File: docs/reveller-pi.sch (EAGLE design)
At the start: 21 parts, among them IC100 6581, Q100 IRF9Z24N, T100 BC547, X100 RASPI_BOARD_AB_E0, X101 PG203J, X102 CANTON-POWER

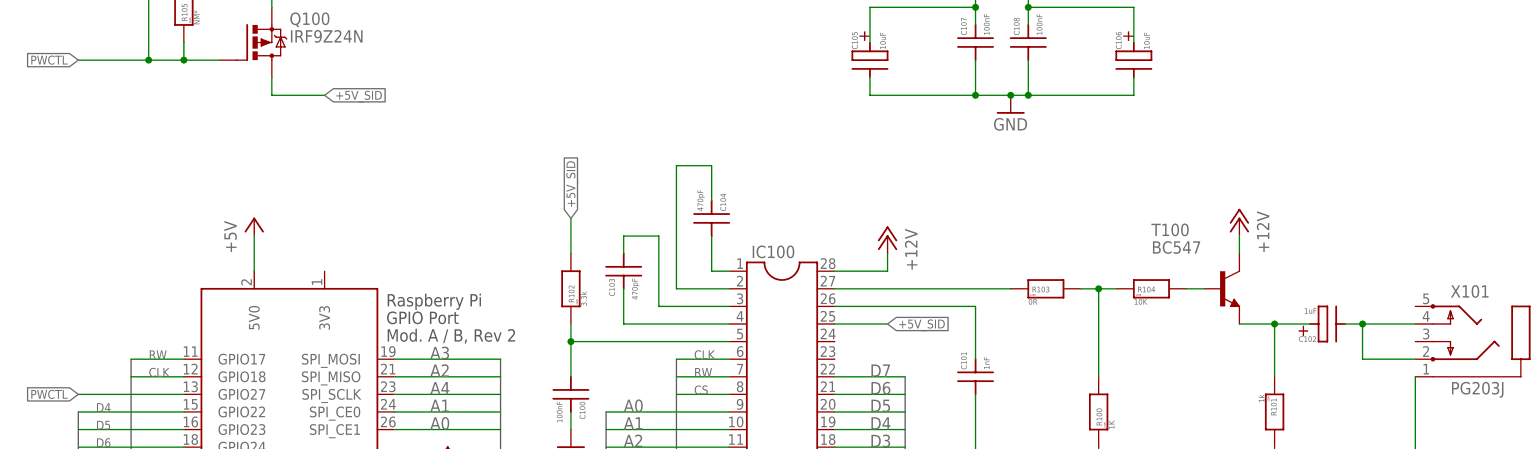
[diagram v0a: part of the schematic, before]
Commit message: Changed schmatic to allow for "stereo" sound
Used wrong pinout on jack connector, thereby giving only mono sound.
Also added one 1000uF capacitor to allow for bad powersupplys to not
kill the raspberrypi during startup of sidchip
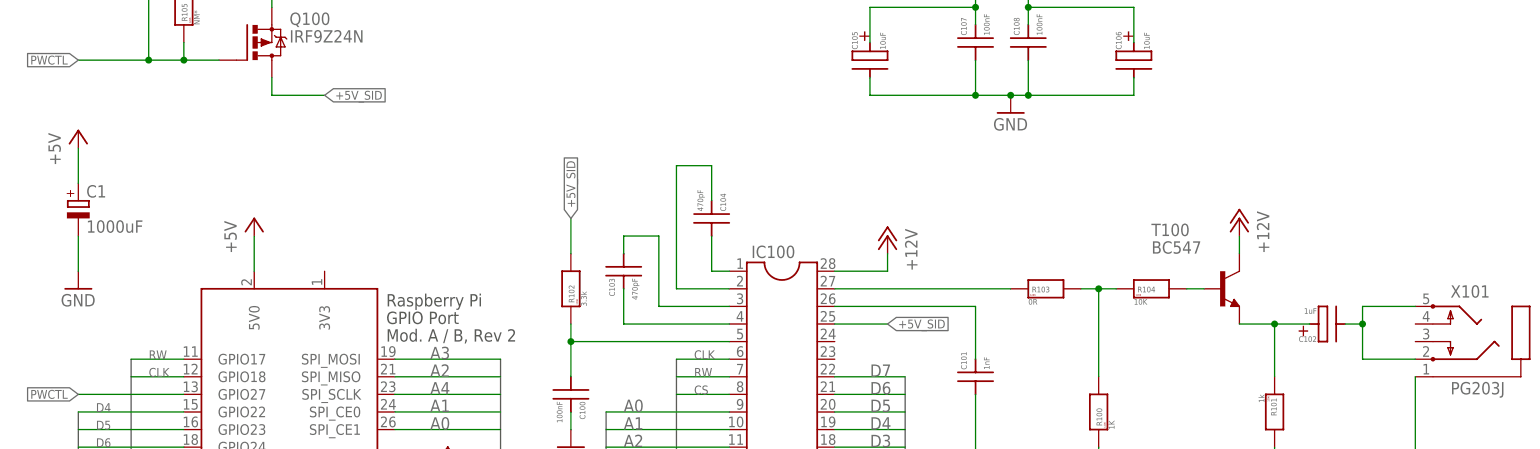
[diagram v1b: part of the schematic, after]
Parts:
- added C1: 1000uF, rcl:CPOL-EUE5-10.5
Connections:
- net +5V: now also C1.+
- net AUDIO_OUT: now also X101.5; no longer X101.4
- net GND: now also C1.-
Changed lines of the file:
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@@
 <?xml version="1.0" encoding="utf-8"?>
 <!DOCTYPE eagle SYSTEM "eagle.dtd">
-<eagle version="6.5.4">
+<eagle version="7.2.0">
 <drawing>
 <settings>
@@
 <grid distance="0.1" unitdist="inch" unit="inch" style="lines" multiple="1" display="no" altdistance="0.01" altunitdist="inch" altunit="inch"/>
 <layers>
-<layer number="1" name="Top" color="4" fill="8" visible="yes" active="no"/>
-<layer number="2" name="Route2" color="1" fill="3" visible="yes" active="no"/>
-<layer number="3" name="Route3" color="4" fill="3" visible="yes" active="no"/>
-<layer number="4" name="Route4" color="1" fill="4" visible="yes" active="no"/>
-<layer number="5" name="Route5" color="4" fill="4" visible="yes" active="no"/>
-<layer number="6" name="Route6" color="1" fill="8" visible="yes" active="no"/>
-<layer number="7" name="Route7" color="4" fill="8" visible="yes" active="no"/>
-<layer number="8" name="Route8" color="1" fill="2" visible="yes" active="no"/>
-<layer number="9" name="Route9" color="4" fill="2" visible="yes" active="no"/>
-<layer number="10" name="Route10" color="1" fill="7" visible="yes" active="no"/>
-<layer number="11" name="Route11" color="4" fill="7" visible="yes" active="no"/>
-<layer number="12" name="Route12" color="1" fill="5" visible="yes" active="no"/>
-<layer number="13" name="Route13" color="4" fill="5" visible="yes" active="no"/>
-<layer number="14" name="Route14" color="1" fill="6" visible="yes" active="no"/>
-<layer number="15" name="Route15" color="4" fill="6" visible="yes" active="no"/>
-<layer number="16" name="Bottom" color="5" fill="8" visible="yes" active="no"/>
-<layer number="17" name="Pads" color="2" fill="1" visible="yes" active="no"/>
-<layer number="18" name="Vias" color="2" fill="1" visible="yes" active="no"/>
-<layer number="19" name="Unrouted" color="6" fill="1" visible="yes" active="no"/>
-<layer number="20" name="Dimension" color="15" fill="1" visible="yes" active="no"/>
-<layer number="21" name="tPlace" color="16" fill="1" visible="yes" active="no"/>
-<layer number="22" name="bPlace" color="14" fill="1" visible="yes" active="no"/>
-<layer number="23" name="tOrigins" color="15" fill="1" visible="yes" active="no"/>
-<layer number="24" name="bOrigins" color="15" fill="1" visible="yes" active="no"/>
-<layer number="25" name="tNames" color="7" fill="1" visible="yes" active="no"/>
-<layer number="26" name="bNames" color="7" fill="1" visible="yes" active="no"/>
-<layer number="27" name="tValues" color="7" fill="1" visible="yes" active="no"/>
-<layer number="28" name="bValues" color="7" fill="1" visible="yes" active="no"/>
+<layer number="1" name="Top" color="4" fill="8" visible="no" active="no"/>
+<layer number="2" name="Route2" color="1" fill="3" visible="no" active="no"/>
+<layer number="3" name="Route3" color="4" fill="3" visible="no" active="no"/>
+<layer number="4" name="Route4" color="1" fill="4" visible="no" active="no"/>
+<layer number="5" name="Route5" color="4" fill="4" visible="no" active="no"/>
+<layer number="6" name="Route6" color="1" fill="8" visible="no" active="no"/>
+<layer number="7" name="Route7" color="4" fill="8" visible="no" active="no"/>
+<layer number="8" name="Route8" color="1" fill="2" visible="no" active="no"/>
+<layer number="9" name="Route9" color="4" fill="2" visible="no" active="no"/>
+<layer number="10" name="Route10" color="1" fill="7" visible="no" active="no"/>
+<layer number="11" name="Route11" color="4" fill="7" visible="no" active="no"/>
+<layer number="12" name="Route12" color="1" fill="5" visible="no" active="no"/>
+<layer number="13" name="Route13" color="4" fill="5" visible="no" active="no"/>
+<layer number="14" name="Route14" color="1" fill="6" visible="no" active="no"/>
+<layer number="15" name="Route15" color="4" fill="6" visible="no" active="no"/>
+<layer number="16" name="Bottom" color="5" fill="8" visible="no" active="no"/>
+<layer number="17" name="Pads" color="2" fill="1" visible="no" active="no"/>
+<layer number="18" name="Vias" color="2" fill="1" visible="no" active="no"/>
+<layer number="19" name="Unrouted" color="6" fill="1" visible="no" active="no"/>
+<layer number="20" name="Dimension" color="15" fill="1" visible="no" active="no"/>
+<layer number="21" name="tPlace" color="16" fill="1" visible="no" active="no"/>
+<layer number="22" name="bPlace" color="14" fill="1" visible="no" active="no"/>
+<layer number="23" name="tOrigins" color="15" fill="1" visible="no" active="no"/>
+<layer number="24" name="bOrigins" color="15" fill="1" visible="no" active="no"/>
+<layer number="25" name="tNames" color="7" fill="1" visible="no" active="no"/>
+<layer number="26" name="bNames" color="7" fill="1" visible="no" active="no"/>
+<layer number="27" name="tValues" color="7" fill="1" visible="no" active="no"/>
+<layer number="28" name="bValues" color="7" fill="1" visible="no" active="no"/>
 <layer number="29" name="tStop" color="7" fill="3" visible="no" active="no"/>
 <layer number="30" name="bStop" color="7" fill="6" visible="no" active="no"/>
@@
 <layer number="35" name="tGlue" color="7" fill="4" visible="no" active="no"/>
 <layer number="36" name="bGlue" color="7" fill="5" visible="no" active="no"/>
-<layer number="37" name="tTest" color="7" fill="1" visible="yes" active="no"/>
-<layer number="38" name="bTest" color="7" fill="1" visible="yes" active="no"/>
+<layer number="37" name="tTest" color="7" fill="1" visible="no" active="no"/>
+<layer number="38" name="bTest" color="7" fill="1" visible="no" active="no"/>
 <layer number="39" name="tKeepout" color="4" fill="11" visible="no" active="no"/>
 <layer number="40" name="bKeepout" color="1" fill="11" visible="no" active="no"/>
@@
 <layer number="44" name="Drills" color="7" fill="1" visible="no" active="no"/>
 <layer number="45" name="Holes" color="7" fill="1" visible="no" active="no"/>
-<layer number="46" name="Milling" color="3" fill="1" visible="yes" active="no"/>
-<layer number="47" name="Measures" color="7" fill="1" visible="yes" active="no"/>
-<layer number="48" name="Document" color="7" fill="1" visible="yes" active="no"/>
-<layer number="49" name="Reference" color="7" fill="1" visible="yes" active="no"/>
-<layer number="50" name="dxf" color="7" fill="1" visible="yes" active="no"/>
-<layer number="51" name="tDocu" color="6" fill="1" visible="yes" active="no"/>
-<layer number="52" name="bDocu" color="7" fill="1" visible="yes" active="no"/>
-<layer number="53" name="tPatch" color="7" fill="9" visible="yes" active="no"/>
-<layer number="54" name="bPatch" color="1" fill="9" visible="yes" active="no"/>
+<layer number="46" name="Milling" color="3" fill="1" visible="no" active="no"/>
+<layer number="47" name="Measures" color="7" fill="1" visible="no" active="no"/>
+<layer number="48" name="Document" color="7" fill="1" visible="no" active="no"/>
+<layer number="49" name="Reference" color="7" fill="1" visible="no" active="no"/>
+<layer number="50" name="dxf" color="7" fill="1" visible="no" active="no"/>
+<layer number="51" name="tDocu" color="6" fill="1" visible="no" active="no"/>
+<layer number="52" name="bDocu" color="7" fill="1" visible="no" active="no"/>
+<layer number="53" name="tPatch" color="7" fill="9" visible="no" active="no"/>
+<layer number="54" name="bPatch" color="1" fill="9" visible="no" active="no"/>
 <layer number="90" name="Modules" color="5" fill="1" visible="yes" active="yes"/>
 <layer number="91" name="Nets" color="2" fill="1" visible="yes" active="yes"/>
@@
 <part name="C108" library="cyviz" deviceset="SMD-IPC_CAP" device="C1206" value="100nF"/>
 <part name="C101" library="cyviz" deviceset="SMD-IPC_CAP" device="C1206" value="1nF"/>
+<part name="C1" library="rcl" deviceset="CPOL-EU" device="E5-10.5" value="1000uF"/>
+<part name="P+1" library="supply1" deviceset="+5V" device=""/>
+<part name="GND1" library="supply1" deviceset="GND" device=""/>
 </parts>
 <sheets>
@@
 <instance part="C108" gate="G$1" x="154.94" y="111.76" rot="R90"/>
 <instance part="C101" gate="G$1" x="147.32" y="63.5" rot="R90"/>
+<instance part="C1" gate="G$1" x="17.78" y="88.9"/>
+<instance part="P+1" gate="1" x="17.78" y="99.06"/>
+<instance part="GND1" gate="1" x="17.78" y="76.2"/>
 </instances>
 <busses>
@@
 <pinref part="C100" gate="G$1" pin="2"/>
 </segment>
+<segment>
+<pinref part="C1" gate="G$1" pin="-"/>
+<pinref part="GND1" gate="1" pin="GND"/>
+<wire x1="17.78" y1="78.74" x2="17.78" y2="83.82" width="0.1524" layer="91"/>
+</segment>
 </net>
 <net name="D0" class="1">
@@
 <wire x1="33.02" y1="124.46" x2="45.72" y2="124.46" width="0.1524" layer="91"/>
 <junction x="45.72" y="124.46"/>
+</segment>
+<segment>
+<pinref part="C1" gate="G$1" pin="+"/>
+<wire x1="17.78" y1="96.52" x2="17.78" y2="91.44" width="0.1524" layer="91"/>
+<pinref part="P+1" gate="1" pin="+5V"/>
 </segment>
 </net>
@@
 <net name="AUDIO_OUT" class="0">
 <segment>
-<pinref part="X101" gate="1" pin="4"/>
-<wire x1="200.66" y1="71.12" x2="203.2" y2="71.12" width="0.1524" layer="91"/>
 <pinref part="X101" gate="1" pin="2"/>
-<wire x1="203.2" y1="71.12" x2="210.82" y2="71.12" width="0.1524" layer="91"/>
 <wire x1="210.82" y1="66.04" x2="203.2" y2="66.04" width="0.1524" layer="91"/>
 <wire x1="203.2" y1="66.04" x2="203.2" y2="71.12" width="0.1524" layer="91"/>
+<pinref part="C102" gate="POS" pin="-"/>
+<wire x1="200.66" y1="71.12" x2="203.2" y2="71.12" width="0.1524" layer="91"/>
+<wire x1="203.2" y1="71.12" x2="203.2" y2="73.66" width="0.1524" layer="91"/>
 <junction x="203.2" y="71.12"/>
-<pinref part="C102" gate="POS" pin="-"/>
-</segment>
-</net>
+<pinref part="X101" gate="1" pin="5"/>
+<wire x1="203.2" y1="73.66" x2="210.82" y2="73.66" width="0.1524" layer="91"/>
+</segment>
+</net>

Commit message: replaced cap with resistor
Switched out Capacitor with resistors as its better.
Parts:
- removed C1: 1000uF, rcl:CPOL-EUE5-10.5
- added R106, R107: 4.7, cyviz:SMD-IPC_RESR1206
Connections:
- new net N$1: R106.1, R107.1, X102-4.S
- net +5V: now also R106.2, R107.2; no longer C1.+, X102-4.S
- net GND: no longer C1.-
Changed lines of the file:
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@@
 <?xml version="1.0" encoding="utf-8"?>
 <!DOCTYPE eagle SYSTEM "eagle.dtd">
-<eagle version="7.2.0">
+<eagle version="7.5.0">
 <drawing>
 <settings>
@@
 <part name="C108" library="cyviz" deviceset="SMD-IPC_CAP" device="C1206" value="100nF"/>
 <part name="C101" library="cyviz" deviceset="SMD-IPC_CAP" device="C1206" value="1nF"/>
-<part name="C1" library="rcl" deviceset="CPOL-EU" device="E5-10.5" value="1000uF"/>
-<part name="P+1" library="supply1" deviceset="+5V" device=""/>
-<part name="GND1" library="supply1" deviceset="GND" device=""/>
+<part name="R107" library="cyviz" deviceset="SMD-IPC_RES" device="R1206" value="4.7"/>
+<part name="R106" library="cyviz" deviceset="SMD-IPC_RES" device="R1206" value="4.7"/>
 </parts>
 <sheets>
@@
 <instance part="GND100" gate="1" x="48.26" y="17.78"/>
 <instance part="GND104" gate="1" x="165.1" y="48.26"/>
-<instance part="P+106" gate="1" x="35.56" y="162.56"/>
-<instance part="P+107" gate="1" x="40.64" y="162.56" rot="MR0"/>
+<instance part="P+106" gate="1" x="35.56" y="172.72"/>
+<instance part="P+107" gate="1" x="40.64" y="172.72" rot="MR0"/>
 <instance part="GND109" gate="1" x="33.02" y="139.7"/>
 <instance part="FRAME100" gate="G$1" x="0" y="0"/>
@@
 <instance part="C108" gate="G$1" x="154.94" y="111.76" rot="R90"/>
 <instance part="C101" gate="G$1" x="147.32" y="63.5" rot="R90"/>
-<instance part="C1" gate="G$1" x="17.78" y="88.9"/>
-<instance part="P+1" gate="1" x="17.78" y="99.06"/>
-<instance part="GND1" gate="1" x="17.78" y="76.2"/>
+<instance part="R107" gate="G$1" x="38.1" y="160.02" rot="R90"/>
+<instance part="R106" gate="G$1" x="33.02" y="160.02" rot="R90"/>
 </instances>
 <busses>
@@
 <pinref part="C100" gate="G$1" pin="2"/>
 </segment>
-<segment>
-<pinref part="C1" gate="G$1" pin="-"/>
-<pinref part="GND1" gate="1" pin="GND"/>
-<wire x1="17.78" y1="78.74" x2="17.78" y2="83.82" width="0.1524" layer="91"/>
-</segment>
 </net>
 <net name="D0" class="1">
@@
 <pinref part="X102" gate="-1" pin="S"/>
 <wire x1="43.18" y1="152.4" x2="40.64" y2="152.4" width="0.1524" layer="91"/>
-<wire x1="40.64" y1="152.4" x2="40.64" y2="160.02" width="0.1524" layer="91"/>
+<wire x1="40.64" y1="152.4" x2="40.64" y2="170.18" width="0.1524" layer="91"/>
 <pinref part="P+107" gate="1" pin="+12V"/>
 </segment>
@@
 <wire x1="43.18" y1="78.74" x2="43.18" y2="83.82" width="0.1524" layer="91"/>
 <pinref part="P+102" gate="1" pin="+5V"/>
-</segment>
-<segment>
-<pinref part="X102" gate="-4" pin="S"/>
-<wire x1="43.18" y1="144.78" x2="35.56" y2="144.78" width="0.1524" layer="91"/>
-<wire x1="35.56" y1="144.78" x2="35.56" y2="160.02" width="0.1524" layer="91"/>
-<pinref part="P+106" gate="1" pin="+5V"/>
 </segment>
 <segment>
@@
 </segment>
 <segment>
-<pinref part="C1" gate="G$1" pin="+"/>
-<wire x1="17.78" y1="96.52" x2="17.78" y2="91.44" width="0.1524" layer="91"/>
-<pinref part="P+1" gate="1" pin="+5V"/>
+<pinref part="R107" gate="G$1" pin="2"/>
+<pinref part="P+106" gate="1" pin="+5V"/>
+<wire x1="38.1" y1="165.1" x2="35.56" y2="165.1" width="0.1524" layer="91"/>
+<wire x1="35.56" y1="165.1" x2="35.56" y2="170.18" width="0.1524" layer="91"/>
+<pinref part="R106" gate="G$1" pin="2"/>
+<wire x1="33.02" y1="165.1" x2="35.56" y2="165.1" width="0.1524" layer="91"/>
+<junction x="35.56" y="165.1"/>
 </segment>
 </net>
@@
 </segment>
 </net>
+<net name="N$1" class="0">
+<segment>
+<pinref part="X102" gate="-4" pin="S"/>
+<wire x1="43.18" y1="144.78" x2="35.56" y2="144.78" width="0.1524" layer="91"/>
+<wire x1="35.56" y1="144.78" x2="35.56" y2="154.94" width="0.1524" layer="91"/>
+<pinref part="R107" gate="G$1" pin="1"/>
+<wire x1="35.56" y1="154.94" x2="38.1" y2="154.94" width="0.1524" layer="91"/>
+<pinref part="R106" gate="G$1" pin="1"/>
+<wire x1="35.56" y1="154.94" x2="33.02" y2="154.94" width="0.1524" layer="91"/>
+<junction x="35.56" y="154.94"/>
+</segment>
+</net>
